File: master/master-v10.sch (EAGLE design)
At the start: 41 parts, among them IC2 DS3231/SO, J1 AVR_SPI_PRG_6PTH, J2 TWIG-2.0-DIPD, J3 TWIG-2.0-DIPD, J4 TWIG-2.0-DIPD, U1 MCP9804, U2 ATMEGA640/1280/2560-A, U3 FT232RL-BASICSSOP, U4 AP1117E, U5 USD-SOCKETNEW, U6 INA169

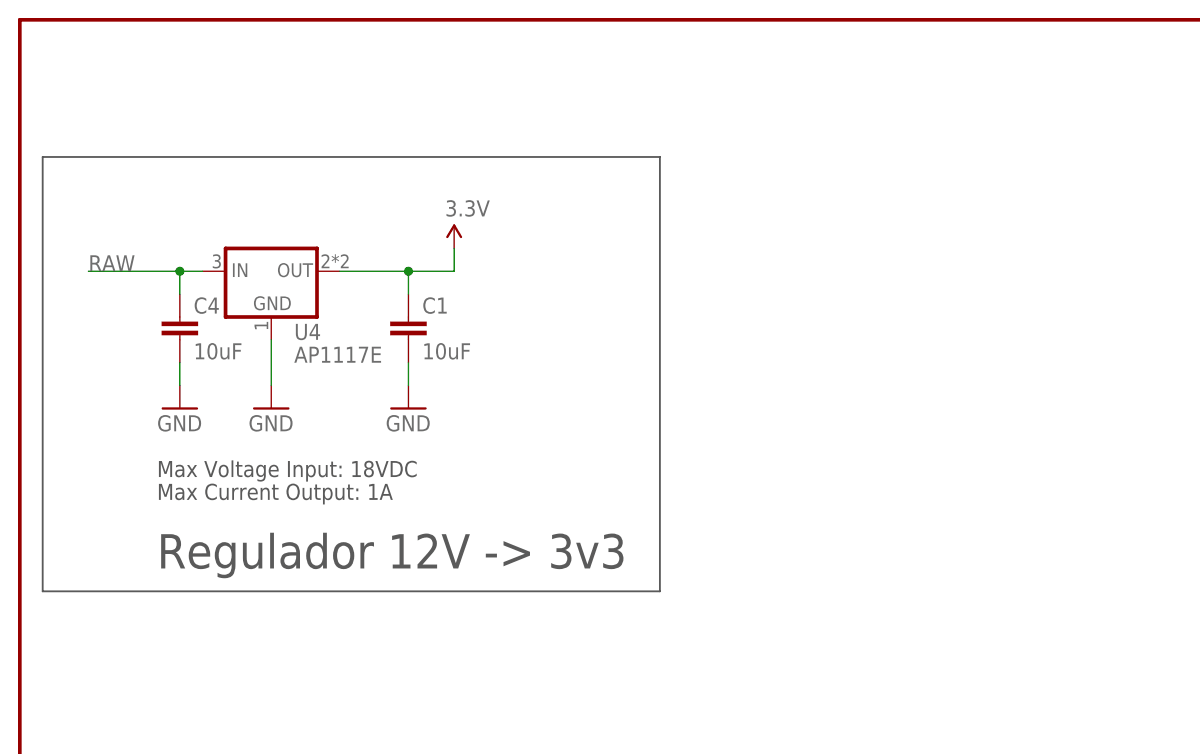
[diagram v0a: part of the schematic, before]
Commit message: 12DC Power Connector and 1st layout
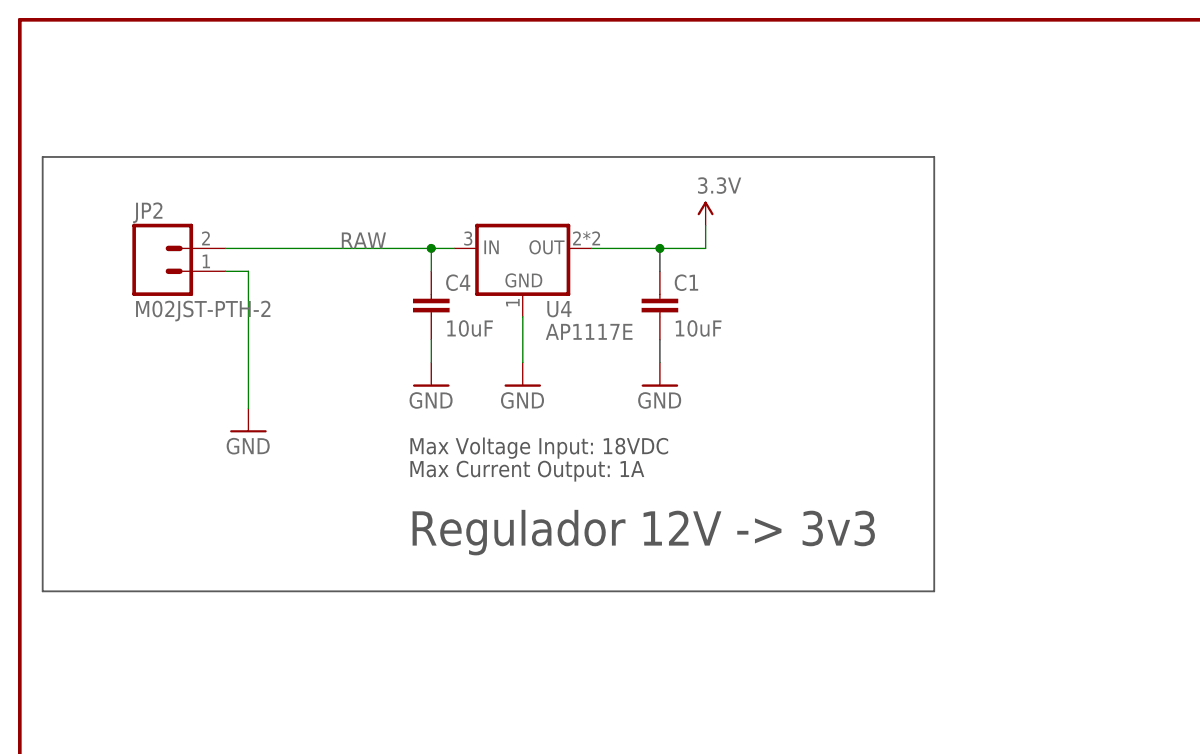
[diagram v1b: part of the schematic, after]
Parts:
- added JP2: M02JST-PTH-2, SparkFun-Connectors:M02JST-PTH-2
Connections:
- net GND: now also JP2.1
- net RAW: now also JP2.2
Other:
- moved on the sheet: C1, C4, U4
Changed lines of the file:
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@@
 <part name="SUPPLY10" library="SparkFun-Aesthetics" deviceset="3.3V" device=""/>
 <part name="U$1" library="resonador" deviceset="RESONATOR-" device="SMD"/>
+<part name="JP2" library="SparkFun-Connectors" deviceset="M02" device="JST-PTH-2"/>
+<part name="GND17" library="SparkFun" deviceset="GND" device=""/>
 </parts>
 <sheets>
 <sheet>
 <plain>
-<text x="15.24" y="228.6" size="1.778" layer="97">Max Voltage Input: 18VDC</text>
-<text x="15.24" y="226.06" size="1.778" layer="97">Max Current Output: 1A</text>
-<text x="15.24" y="218.44" size="3.81" layer="97">Regulador 12V -&gt; 3v3 </text>
+<text x="43.18" y="231.14" size="1.778" layer="97">Max Voltage Input: 18VDC</text>
+<text x="43.18" y="228.6" size="1.778" layer="97">Max Current Output: 1A</text>
+<text x="43.18" y="220.98" size="3.81" layer="97">Regulador 12V -&gt; 3v3 </text>
 <wire x1="2.54" y1="91.44" x2="76.2" y2="91.44" width="0.2032" layer="97"/>
 <wire x1="76.2" y1="91.44" x2="76.2" y2="33.02" width="0.2032" layer="97"/>
 <wire x1="76.2" y1="33.02" x2="2.54" y2="33.02" width="0.2032" layer="97"/>
 <wire x1="2.54" y1="33.02" x2="2.54" y2="91.44" width="0.2032" layer="97"/>
-<wire x1="2.54" y1="264.16" x2="71.12" y2="264.16" width="0.2032" layer="97"/>
-<wire x1="71.12" y1="264.16" x2="71.12" y2="215.9" width="0.2032" layer="97"/>
-<wire x1="71.12" y1="215.9" x2="2.54" y2="215.9" width="0.2032" layer="97"/>
+<wire x1="2.54" y1="264.16" x2="101.6" y2="264.16" width="0.2032" layer="97"/>
+<wire x1="101.6" y1="264.16" x2="101.6" y2="215.9" width="0.2032" layer="97"/>
+<wire x1="101.6" y1="215.9" x2="2.54" y2="215.9" width="0.2032" layer="97"/>
 <wire x1="2.54" y1="215.9" x2="2.54" y2="264.16" width="0.2032" layer="97"/>
 <text x="30.48" y="35.56" size="3.81" layer="97">RTC + Bateria</text>
@@
 </plain>
 <instances>
-<instance part="GND25" gate="1" x="43.18" y="236.22"/>
+<instance part="GND25" gate="1" x="71.12" y="238.76"/>
 <instance part="GND5" gate="1" x="172.72" y="66.04"/>
 <instance part="C2" gate="G$1" x="154.94" y="241.3" smashed="yes" rot="R270">
@@
 <instance part="R1" gate="G$1" x="266.7" y="205.74" rot="R270"/>
 <instance part="GND2" gate="1" x="266.7" y="172.72"/>
-<instance part="C1" gate="G$1" x="43.18" y="243.84"/>
-<instance part="C4" gate="G$1" x="17.78" y="243.84"/>
-<instance part="GND3" gate="1" x="17.78" y="236.22"/>
-<instance part="GND6" gate="1" x="27.94" y="236.22"/>
+<instance part="C1" gate="G$1" x="71.12" y="246.38"/>
+<instance part="C4" gate="G$1" x="45.72" y="246.38"/>
+<instance part="GND3" gate="1" x="45.72" y="238.76"/>
+<instance part="GND6" gate="1" x="55.88" y="238.76"/>
 <instance part="R3" gate="G$1" x="160.02" y="109.22" rot="R90"/>
 <instance part="IC2" gate="G$1" x="25.4" y="60.96"/>
@@
 </instance>
 <instance part="GND1" gate="1" x="302.26" y="243.84"/>
-<instance part="SUPPLY1" gate="G$1" x="48.26" y="254"/>
+<instance part="SUPPLY1" gate="G$1" x="76.2" y="256.54"/>
 <instance part="SUPPLY2" gate="G$1" x="165.1" y="261.62"/>
 <instance part="SUPPLY3" gate="G$1" x="7.62" y="81.28"/>
@@
 <instance part="FRAME1" gate="G$1" x="0" y="0"/>
 <instance part="FRAME1" gate="G$2" x="330.2" y="0"/>
-<instance part="U4" gate="G$1" x="27.94" y="251.46"/>
+<instance part="U4" gate="G$1" x="55.88" y="254"/>
 <instance part="GND18" gate="1" x="147.32" y="215.9"/>
 <instance part="R10" gate="G$1" x="292.1" y="154.94"/>
@@
 <instance part="SUPPLY10" gate="G$1" x="294.64" y="175.26" rot="R180"/>
 <instance part="U$1" gate="G$1" x="160.02" y="228.6" rot="R270"/>
+<instance part="JP2" gate="G$1" x="15.24" y="251.46"/>
+<instance part="GND17" gate="1" x="25.4" y="233.68"/>
 </instances>
 <busses>
@@
 <net name="GND" class="1">
 <segment>
-<wire x1="43.18" y1="238.76" x2="43.18" y2="241.3" width="0.1524" layer="91"/>
+<wire x1="71.12" y1="241.3" x2="71.12" y2="243.84" width="0.1524" layer="91"/>
 <pinref part="GND25" gate="1" pin="GND"/>
 <pinref part="C1" gate="G$1" pin="2"/>
@@
 <pinref part="C4" gate="G$1" pin="2"/>
 <pinref part="GND3" gate="1" pin="GND"/>
-<wire x1="17.78" y1="241.3" x2="17.78" y2="238.76" width="0.1524" layer="91"/>
+<wire x1="45.72" y1="243.84" x2="45.72" y2="241.3" width="0.1524" layer="91"/>
 </segment>
 <segment>
 <pinref part="GND6" gate="1" pin="GND"/>
-<wire x1="27.94" y1="238.76" x2="27.94" y2="243.84" width="0.1524" layer="91"/>
+<wire x1="55.88" y1="241.3" x2="55.88" y2="246.38" width="0.1524" layer="91"/>
 <pinref part="U4" gate="G$1" pin="GND"/>
 </segment>
@@
 <wire x1="294.64" y1="185.42" x2="299.72" y2="185.42" width="0.1524" layer="91"/>
 </segment>
+<segment>
+<pinref part="GND17" gate="1" pin="GND"/>
+<wire x1="25.4" y1="236.22" x2="25.4" y2="251.46" width="0.1524" layer="91"/>
+<pinref part="JP2" gate="G$1" pin="1"/>
+<wire x1="25.4" y1="251.46" x2="22.86" y2="251.46" width="0.1524" layer="91"/>
+</segment>
 </net>
 <net name="SCK" class="0">
@@
 <net name="RAW" class="1">
 <segment>
-<wire x1="7.62" y1="251.46" x2="17.78" y2="251.46" width="0.1524" layer="91"/>
-<label x="7.62" y="251.46" size="1.778" layer="95"/>
+<wire x1="22.86" y1="254" x2="45.72" y2="254" width="0.1524" layer="91"/>
+<label x="35.56" y="254" size="1.778" layer="95"/>
 <pinref part="C4" gate="G$1" pin="1"/>
-<wire x1="17.78" y1="251.46" x2="20.32" y2="251.46" width="0.1524" layer="91"/>
-<wire x1="17.78" y1="248.92" x2="17.78" y2="251.46" width="0.1524" layer="91"/>
-<junction x="17.78" y="251.46"/>
+<wire x1="45.72" y1="254" x2="48.26" y2="254" width="0.1524" layer="91"/>
+<wire x1="45.72" y1="251.46" x2="45.72" y2="254" width="0.1524" layer="91"/>
+<junction x="45.72" y="254"/>
 <pinref part="U4" gate="G$1" pin="IN"/>
+<pinref part="JP2" gate="G$1" pin="2"/>
 </segment>
 <segment>
@@
 <net name="3.3V" class="0">
 <segment>
-<wire x1="43.18" y1="251.46" x2="48.26" y2="251.46" width="0.1524" layer="91"/>
-<wire x1="48.26" y1="251.46" x2="48.26" y2="254" width="0.1524" layer="91"/>
-<wire x1="43.18" y1="251.46" x2="43.18" y2="248.92" width="0.1524" layer="91"/>
+<wire x1="71.12" y1="254" x2="76.2" y2="254" width="0.1524" layer="91"/>
+<wire x1="76.2" y1="254" x2="76.2" y2="256.54" width="0.1524" layer="91"/>
+<wire x1="71.12" y1="254" x2="71.12" y2="251.46" width="0.1524" layer="91"/>
 <pinref part="C1" gate="G$1" pin="1"/>
-<wire x1="43.18" y1="251.46" x2="35.56" y2="251.46" width="0.1524" layer="91"/>
-<junction x="43.18" y="251.46"/>
+<wire x1="71.12" y1="254" x2="63.5" y2="254" width="0.1524" layer="91"/>
+<junction x="71.12" y="254"/>
 <pinref part="SUPPLY1" gate="G$1" pin="3.3V"/>
 <pinref part="U4" gate="G$1" pin="OUT"/>

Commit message: agregados pads
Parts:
- added V_IN, V_OUT: MOUNT-PAD-ROUND3.0, holes:MOUNT-PAD-ROUND3.0
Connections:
- net VIN+: now also V_IN.MOUNT
- net VIN-: now also V_OUT.MOUNT
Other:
- moved on the sheet: R14
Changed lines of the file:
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@@
 <part name="JP2" library="SparkFun-Connectors" deviceset="M02" device="JST-PTH-2"/>
 <part name="GND17" library="SparkFun" deviceset="GND" device=""/>
+<part name="V_OUT" library="holes" deviceset="MOUNT-PAD-ROUND" device="3.0"/>
+<part name="V_IN" library="holes" deviceset="MOUNT-PAD-ROUND" device="3.0"/>
 </parts>
 <sheets>
@@
 <instance part="C7" gate="G$1" x="297.18" y="228.6" rot="R270"/>
 <instance part="GND4" gate="1" x="287.02" y="228.6" rot="R270"/>
-<instance part="R14" gate="G$1" x="373.38" y="261.62"/>
+<instance part="R14" gate="G$1" x="375.92" y="261.62"/>
 <instance part="R15" gate="G$1" x="383.54" y="251.46" rot="R90"/>
 <instance part="GND22" gate="1" x="383.54" y="238.76"/>
@@
 <instance part="JP2" gate="G$1" x="15.24" y="251.46"/>
 <instance part="GND17" gate="1" x="25.4" y="233.68"/>
+<instance part="V_OUT" gate="G$1" x="355.6" y="238.76"/>
+<instance part="V_IN" gate="G$1" x="355.6" y="269.24"/>
 </instances>
 <busses>
@@
 <segment>
 <pinref part="R14" gate="G$1" pin="1"/>
-<wire x1="368.3" y1="261.62" x2="363.22" y2="261.62" width="0.1524" layer="91"/>
-<label x="363.22" y="261.62" size="1.27" layer="95" rot="R180" xref="yes"/>
+<wire x1="370.84" y1="261.62" x2="368.3" y2="261.62" width="0.1524" layer="91"/>
+<label x="368.3" y="261.62" size="1.27" layer="95" rot="R180" xref="yes"/>
 </segment>
 <segment>
@@
 <wire x1="342.9" y1="251.46" x2="350.52" y2="251.46" width="0.1524" layer="91"/>
 <wire x1="350.52" y1="251.46" x2="350.52" y2="256.54" width="0.1524" layer="91"/>
-<wire x1="350.52" y1="256.54" x2="355.6" y2="256.54" width="0.1524" layer="91"/>
+<wire x1="350.52" y1="256.54" x2="353.06" y2="256.54" width="0.1524" layer="91"/>
 <pinref part="R12" gate="G$1" pin="2"/>
 <pinref part="U6" gate="G$1" pin="VIN+"/>
+<pinref part="V_IN" gate="G$1" pin="MOUNT"/>
+<wire x1="353.06" y1="256.54" x2="355.6" y2="256.54" width="0.1524" layer="91"/>
+<wire x1="353.06" y1="269.24" x2="353.06" y2="256.54" width="0.1524" layer="91"/>
 </segment>
 </net>
 <net name="VIN-" class="0">
 <segment>
-<wire x1="342.9" y1="246.38" x2="355.6" y2="246.38" width="0.1524" layer="91"/>
+<wire x1="342.9" y1="246.38" x2="353.06" y2="246.38" width="0.1524" layer="91"/>
 <pinref part="R12" gate="G$1" pin="1"/>
 <pinref part="U6" gate="G$1" pin="VIN-"/>
+<pinref part="V_OUT" gate="G$1" pin="MOUNT"/>
+<wire x1="353.06" y1="246.38" x2="355.6" y2="246.38" width="0.1524" layer="91"/>
+<wire x1="353.06" y1="238.76" x2="353.06" y2="246.38" width="0.1524" layer="91"/>
 </segment>
 </net>
@@
 <pinref part="R14" gate="G$1" pin="2"/>
 <pinref part="R15" gate="G$1" pin="2"/>
-<wire x1="378.46" y1="261.62" x2="383.54" y2="261.62" width="0.1524" layer="91"/>
+<wire x1="381" y1="261.62" x2="383.54" y2="261.62" width="0.1524" layer="91"/>
 <wire x1="383.54" y1="261.62" x2="383.54" y2="256.54" width="0.1524" layer="91"/>
 <wire x1="383.54" y1="261.62" x2="388.62" y2="261.62" width="0.1524" layer="91"/>
